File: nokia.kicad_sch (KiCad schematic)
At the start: 21 parts, among them J1 Conn_01x07, J3 Conn_01x04_Pin, J4 Conn_01x04, M1 Motor_DC, SW1 SW_Push, U1 Pico

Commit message: 2nd iteration of board
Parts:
- removed J3: Conn_01x04_Pin, Battery:battery, symbol Connector:Conn_01x04_Pin
- removed J4: Conn_01x04, Connector_PinHeader_2.54mm:PinHeader_1x04_P2.54mm_Vertical, symbol Connector_Generic:Conn_01x04
- removed U1: Pico, MCU_RaspberryPi_and_Boards:RPi_Pico_SMD_TH, symbol MCU_RaspberryPi_and_Boards:Pico
- added C1, C19, C5: 10u, Capacitor_SMD:C_0805_2012Metric, symbol Device:C
- added C10, C6, C7, C9: 4.7u, Capacitor_SMD:C_0402_1005Metric, symbol Device:C
- added C11, C12, C13, C14, C15, C16, C17, C18, C2, C20, C21, C8: 100n, Capacitor_SMD:C_0402_1005Metric, symbol Device:C
- added C3, C4: 15p, Capacitor_SMD:C_0402_1005Metric, symbol Device:C
- added J2: USB_B_Micro, Connector_USB:USB_Micro-B_Amphenol_10103594-0001LF_Horizontal, symbol Connector:USB_B_Micro
- added J20: Conn_01x04_Pin, Battery:battery, symbol Connector:Conn_01x04_Pin
- added J3, J6: SM03B-SRSS-TB, Connector_JST:JST_SH_SM03B-SRSS-TB_1x03-1MP_P1.00mm_Horizontal, symbol Connector_Generic_MountingPin:Conn_01x03_MountingPin
- added J4: Conn_01x06_Pin, Connector:sim connector connector, symbol Connector:SIM_Card
- added J5: Conn_02x06_Top_Bottom, Connector_PinHeader_2.54mm:PinHeader_2x06_P2.54mm_Vertical_SMD, symbol Connector_Generic:Conn_02x06_Top_Bottom
- added JP17: SolderJumper_2_Open, Jumper:SolderJumper-2_P1.3mm_Open_RoundedPad1.0x1.5mm, symbol Jumper:SolderJumper_2_Open
- added KPDOWN1, KPSELECT1, KPUP1: Jumper_2_Open, Jumper:ButtonPads, symbol Jumper:Jumper_2_Open
- added L1: 3.3u, RP2350_80QFN_minimal:L_pol_2016, symbol Device:L
- added R1, R9: DNF, Resistor_SMD:R_0402_1005Metric, symbol Device:R
- added R10: 0, Resistor_SMD:R_0402_1005Metric, symbol Device:R
- added R2, R6: 1k, Resistor_SMD:R_0402_1005Metric, symbol Device:R
- added R3: 33, Resistor_SMD:R_0402_1005Metric, symbol Device:R
- added R7, R8: 27, Resistor_SMD:R_0402_1005Metric, symbol Device:R
- added U1: W25Q128JVS, Package_SO:SOIC-8_5.23x5.23mm_P1.27mm, symbol Memory_Flash:W25Q128JVS
- added U4: NCP1117-3.3_SOT223, Package_TO_SOT_SMD:SOT-223-3_TabPin2, symbol Regulator_Linear:NCP1117-3.3_SOT223
- added U5: RP2350_80QFN, RP2350_80QFN_minimal:RP2350-QFN-80-1EP_10x10_P0.4mm_EP3.4x3.4mm_ThermalVias, symbol MCU_RaspberryPi_RP2350:RP2350_80QFN
- added Y1: ABM8-272-T3, Crystal:Crystal_SMD_3225-4Pin_3.2x2.5mm, symbol Device:Crystal_GND24
- C79: renamed from C1; value C -> 100nF; footprint (none) -> Capacitor_SMD:C_0402_1005Metric
- renumbered JP12 to KP#1, JP10 to KP*1, JP11 to KP0, JP1 to KP1, JP2 to KP2, JP3 to KP3, JP4 to KP4, JP5 to KP5, JP6 to KP6, JP7 to KP7, JP8 to KP8, JP9 to KP9, JP13 to KPC1
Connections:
- net +3V3: now also KP#1.1 (A), KP*1.1 (A), KP1.1 (A), KP2.1 (A), KP3.1 (A), KP4.1 (A), KP6.1 (A), KP7.1 (A), KP8.1 (A), KP9.1 (A), C12.1, C13.1, C14.1, C15.1, C16.1, C17.1, C18.1, C19.1, C2.1, C20.1, C21.1, C5.1, C6.1, J20.1 (Pin_1), J4.1 (VCC), KPDOWN1.1 (A), KPSELECT1.1 (A), KPUP1.1 (A), R1.1, R3.1, U1.8 (VCC), U4.2 (VO), U5.15 (IOVDD), U5.24 (IOVDD), U5.29 (IOVDD), U5.41 (IOVDD), U5.5 (IOVDD), U5.50 (IOVDD), U5.59 (ADC_AVDD), U5.60 (IOVDD), U5.64 (VREG_VIN), U5.68 (USB_OTP_VDD), U5.69 (QSPI_IOVDD), U5.76 (IOVDD); no longer KP#1.2 (B), KP*1.2 (B), KP1.2 (B), KP2.2 (B), KP3.2 (B), KP4.2 (B), KP6.2 (B), KP7.2 (B), KP8.2 (B), KP9.2 (B)
- net GND: now also LS2.2, M1.2 (-), C1.2, C10.2, C11.2, C12.2, C13.2, C14.2, C15.2, C16.2, C17.2, C18.2, C19.2, C2.2, C20.2, C21.2, C3.2, C4.2, C5.2, C6.2, C7.2, C8.2, C9.2, J2.5 (GND), J2.6 (Shield), J20.4 (Pin_4), J3.2 (Pin_2), J3.MP (MountPin), J4.5 (GND), J5.9 (Pin_9), J6.2 (Pin_2), J6.MP (MountPin), R6.2, U1.4 (GND), U4.1 (GND), U5.62 (VREG_PGND), U5.81 (GND), Y1.2, Y1.4; no longer SW1.1
- net GPIO16: now reaches KPC1.2 (B)
- net GPIO16: now also U5.16 (GPIO16)
- net GPIO33: now reaches J1.8 (Pin_8)
- net GPIO33: now also J5.7 (Pin_7), U5.42 (GPIO33)
- net GPIO10: now reaches KP0.2 (B)
- net GPIO10: now also U5.8 (GPIO10)
- net GPIO36: now reaches J1.4 (Pin_4)
- net GPIO36: now also J5.11 (Pin_11), U5.45 (GPIO36)
- net GPIO37: now reaches J1.5 (Pin_5)
- net GPIO37: now also J5.10 (Pin_10), U5.46 (GPIO37)
- net GPIO38: now reaches J1.2 (Pin_2)
- net GPIO38: now also U5.47 (GPIO38)
- net GPIO39: now reaches J1.3 (Pin_3)
- net GPIO39: now also J5.12 (Pin_12), U5.48 (GPIO39)
- net RUN: now reaches SW1.2
- net RUN: now also U5.35 (RUN)
- net GPIO2: now reaches M1.1 (+)
- net GPIO2: now also U5.79 (GPIO2)
- net GPIO21: now reaches LS2.1
- net GPIO21: now also U5.21 (GPIO21)
- net GPIO14: now reaches KP5.2 (B)
- net GPIO14: now also U5.13 (GPIO14)
- net at J1.7 (Pin_7): now also J5.8 (Pin_8), JP17.1 (A); no longer C79.2
- new net: R8.2, U5.66 (USB_DM)
- new net: C4.1, R2.2, Y1.3
- new net: R6.1, SW1.1
- new net: C79.2, JP17.2 (B)
- new net: R7.2, U5.67 (USB_DP)
- new net +1V1: C10.1, C11.1, C7.1, C8.1, L1.1, U5.10 (DVDD), U5.32 (DVDD), U5.51 (DVDD), U5.65 (VREG_FB)
- new net FLASH_SS: R1.2, R10.2, R9.2, U1.1 (~{CS})
- new net GPIO0: J3.3 (Pin_3), R9.1, U5.77 (GPIO0)
- new net GPIO1: J3.1 (Pin_1), U5.78 (GPIO1)
- new net GPIO11: KP8.2 (B), U5.9 (GPIO11)
- new net GPIO12: KPSELECT1.2 (B), U5.11 (GPIO12)
- new net GPIO13: KP2.2 (B), U5.12 (GPIO13)
- new net GPIO15: J4.3 (CLK), U5.14 (GPIO15)
- new net GPIO17: KP1.2 (B), U5.17 (GPIO17)
- new net GPIO18: KP4.2 (B), U5.18 (GPIO18)
- new net GPIO19: KP7.2 (B), U5.19 (GPIO19)
- new net GPIO20: KP*1.2 (B), U5.20 (GPIO20)
- new net GPIO22: J4.7 (I/O), U5.22 (GPIO22)
- new net GPIO23: J4.2 (RST), U5.23 (GPIO23)
- new net GPIO24: U5.25 (GPIO24)
- new net GPIO25: U5.26 (GPIO25)
- new net GPIO26: U5.27 (GPIO26)
- new net GPIO27: U5.28 (GPIO27)
- new net GPIO28: U5.36 (GPIO28)
- new net GPIO29: U5.37 (GPIO29)
- new net GPIO3: U5.80 (GPIO3)
- new net GPIO30: U5.38 (GPIO30)
- new net GPIO31: U5.39 (GPIO31)
- new net GPIO32: U5.40 (GPIO32)
- new net GPIO34: U5.43 (GPIO34)
- new net GPIO35: U5.44 (GPIO35)
- new net GPIO4: KP#1.2 (B), U5.1 (GPIO4)
- new net GPIO40_ADC0: U5.49 (GPIO40_ADC0)
- new net GPIO41_ADC1: U5.52 (GPIO41_ADC1)
- new net GPIO42_ADC2: U5.53 (GPIO42_ADC2)
- new net GPIO43_ADC3: U5.54 (GPIO43_ADC3)
- new net GPIO44_ADC4: U5.55 (GPIO44_ADC4)
- new net GPIO45_ADC5: U5.56 (GPIO45_ADC5)
- new net GPIO46_ADC6: U5.57 (GPIO46_ADC6)
- new net GPIO47_ADC7: U5.58 (GPIO47_ADC7)
- new net GPIO5: KP9.2 (B), U5.2 (GPIO5)
- new net GPIO6: KP6.2 (B), U5.3 (GPIO6)
- new net GPIO7: KP3.2 (B), U5.4 (GPIO7)
- new net GPIO8: KPDOWN1.2 (B), U5.6 (GPIO8)
- new net GPIO9: KPUP1.2 (B), U5.7 (GPIO9)
- new net QSPI_SCLK: U1.6 (CLK), U5.71 (QSPI_SCLK)
- new net QSPI_SD0: U1.5 (DI(IO0)), U5.72 (QSPI_SD0)
- new net QSPI_SD1: U1.2 (DO(IO1)), U5.74 (QSPI_SD1)
- new net QSPI_SD2: U1.3 (IO2), U5.73 (QSPI_SD2)
- new net QSPI_SD3: U1.7 (IO3), U5.70 (QSPI_SD3)
- new net QSPI_SS: R10.1, U5.75 (QSPI_SS)
- new net SWCLK: J6.1 (Pin_1), U5.33 (SWCLK)
- new net SWD: J6.3 (Pin_3), U5.34 (SWD)
- new net USB_D+: J2.3 (D+), R7.1
- new net USB_D-: J2.2 (D-), R8.1
- new net VBUS: C1.1, J2.1 (VBUS), U4.3 (VI)
- new net VREG_AVDD: C9.1, R3.2, U5.61 (VREG_AVDD)
- new net VREG_LX: L1.2, U5.63 (VREG_LX)
- new net XIN: C3.1, U5.30 (XIN), Y1.1
- new net XOUT: R2.1, U5.31 (XOUT)
- no-connect marks 0 -> 3
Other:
- note added: "12MHz Crystal"
- note added: "Battery Connection"
- note added: "Display and Misc. GPIO Connection"
- note added: "Flash"
- note added: "JST Debug Connector"
- note added: "Keypad"
- note added: "Make sure R7 and R8 are close to RP2350"
- note added: "Power"
- note added: "SIM Card Tray Connector"
- note added: "UART Connector"
- moved on the sheet: C79, J1, KP#1, KP*1, KP0, KP1, KP2, KP3, KP4, KP5, KP6, KP7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

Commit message: 2nd iteration of board
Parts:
- removed J5: Conn_02x06_Top_Bottom, Connector_PinHeader_2.54mm:PinHeader_2x06_P2.54mm_Vertical_SMD, symbol Connector_Generic:Conn_02x06_Top_Bottom
- added D1: D, symbol Device:D
- added D2, D3, D4, D5, D6, D7, D8, D9: LED_ARGB, LED_SMD:RGBLED-reverse, symbol Device:LED_ARGB
- added Q1: BC847, Package_TO_SOT_SMD:SOT-23, symbol Transistor_BJT:BC847
- added R11, R12, R14, R15, R16, R17, R19, R20, R22, R23, R25, R26, R28, R29, R31, R32: 90, Resistor_SMD:R_0402_1005Metric, symbol Device:R
- added R13, R18, R21, R24, R27, R30, R4, R5: 140, Resistor_SMD:R_0402_1005Metric, symbol Device:R
- LS2: value Speaker_Crystal -> Buzzer
- M1: value Motor_DC -> Vibration
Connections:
- net +3V3: now also M1.1 (+), D1.1 (K), D2.2, D3.2 (A), D4.2 (A), D5.2 (A), D6.2 (A), D7.2 (A), D8.2 (A), D9.2 (A)
- net GND: now also Q1.2 (E); no longer M1.2 (-)
- net GPIO2: now also Q1.1 (B); no longer M1.1 (+)
- net GPIO30: now also R13.2, R18.2, R21.2, R24.2, R27.2, R30.2, R4.2, R5.2
- net GPIO32: now also R11.1, R14.1, R16.1, R19.1, R22.1, R25.1, R28.1, R31.1
- net GPIO34: now also R12.1, R15.1, R17.1, R20.1, R23.1, R26.1, R29.1, R32.1
- new net: D5.3 (GK), R31.2
- new net: D4.4 (BK), R29.2
- new net: D5.4 (BK), R32.2
- new net: D6.3 (GK), R16.2
- new net: D7.4 (BK), R12.2
- new net: D1.2 (A), M1.2 (-), Q1.3 (C)
- new net: D3.1 (RK), R24.1
- new net: D8.1 (RK), R18.1
- new net: D8.3 (GK), R19.2
- new net: D8.4 (BK), R20.2
- new net: D4.1 (RK), R27.1
- new net: D9.4 (BK), R15.2
- new net: D2.1, R21.1
- new net: D2.3 (GK), R22.2
- new net: D2.4 (BK), R23.2
- new net: D3.3 (GK), R25.2
- new net: D3.4 (BK), R26.2
- new net: D4.3 (GK), R28.2
- new net: D5.1 (RK), R30.1
- new net: D7.1 (RK), R4.1
- new net: D7.3 (GK), R11.2
- new net: D6.1 (RK), R5.1
- new net: D6.4 (BK), R17.2
- new net: D9.1 (RK), R13.1
- new net: D9.3 (GK), R14.2
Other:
- moved on the sheet: C1, C2, C3, C4, C5, C79, J2, J20, J3, J4, J6, JP17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

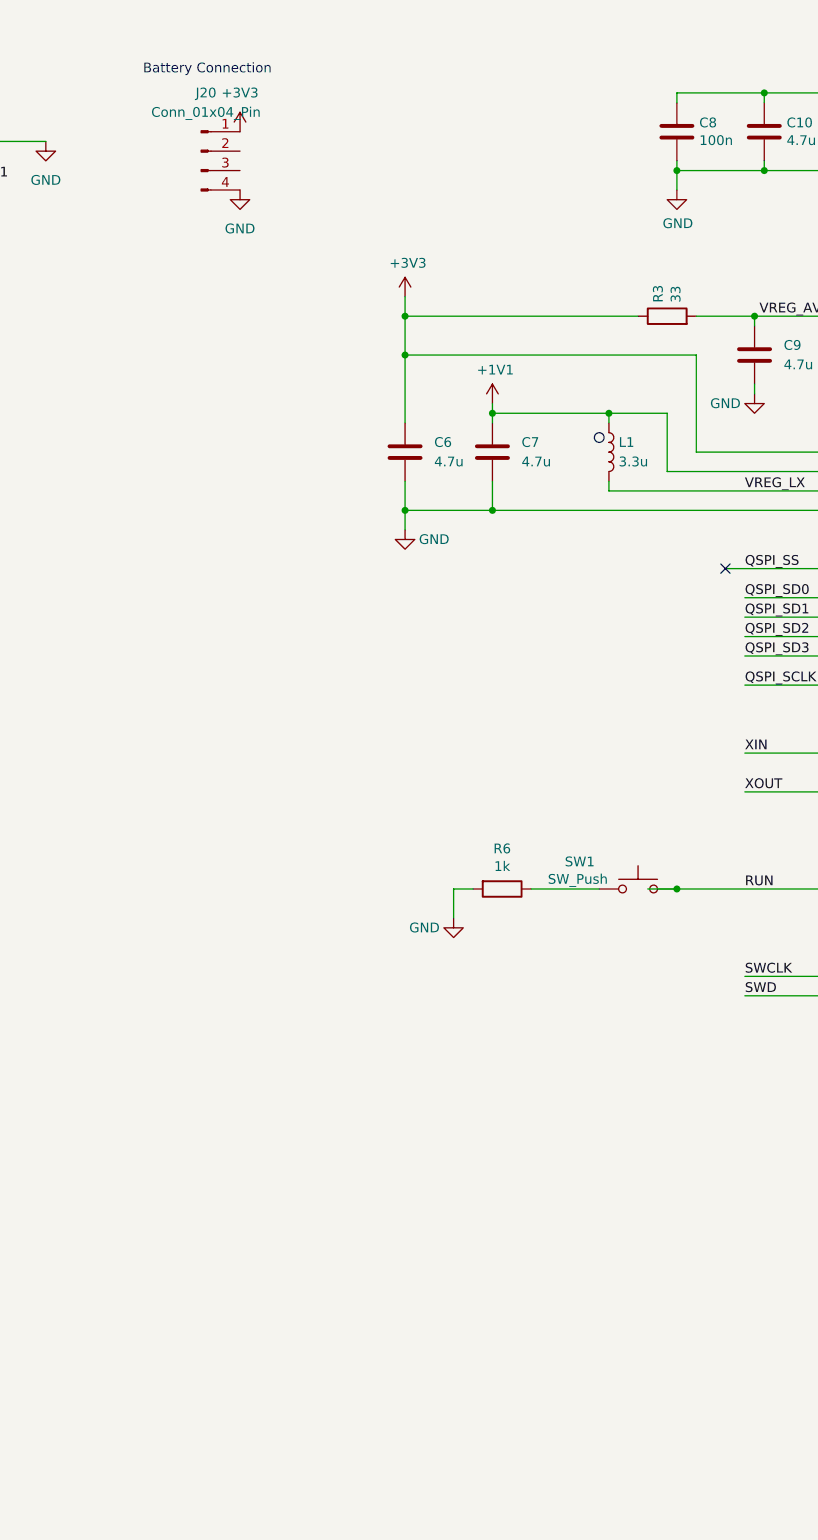
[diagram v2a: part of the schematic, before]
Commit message: add breakout connector
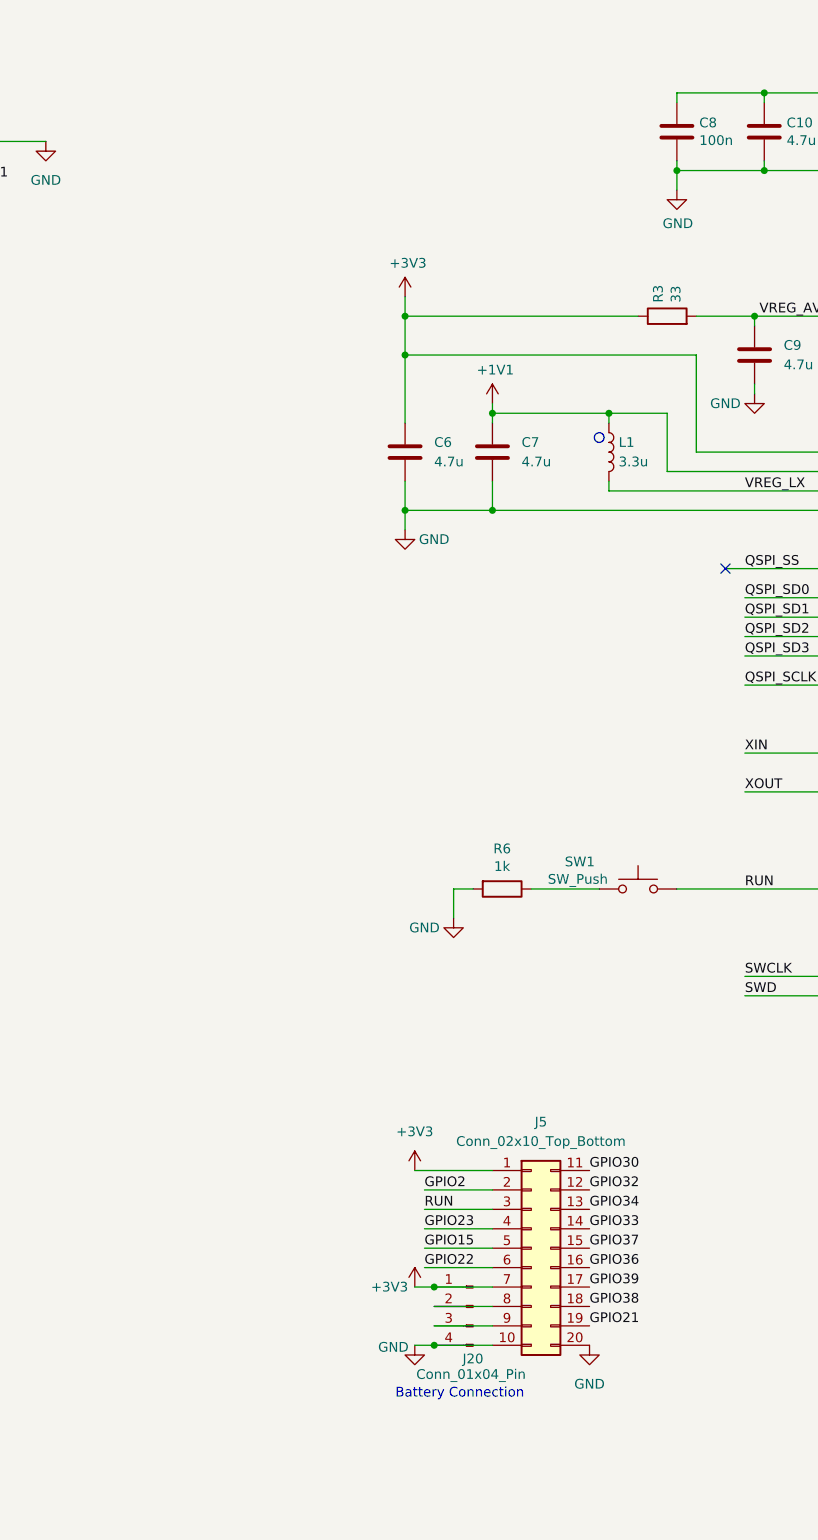
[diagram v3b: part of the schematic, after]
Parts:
- added J5: Conn_02x10_Top_Bottom, Connector_PinHeader_2.54mm:PinHeader_2x10_P2.54mm_Vertical_SMD, symbol Connector_Generic:Conn_02x10_Top_Bottom
- D1: footprint (none) -> Diode_SMD:D_0402_1005Metric
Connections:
- net +3V3: now also J5.1 (Pin_1), J5.7 (Pin_7)
- net GND: now also J5.10 (Pin_10), J5.20 (Pin_20)
- net GPIO15: now also J5.5 (Pin_5)
- net GPIO2: now also J5.2 (Pin_2)
- net GPIO21: now also J5.19 (Pin_19)
- net GPIO22: now also J5.6 (Pin_6)
- net GPIO23: now also J5.4 (Pin_4)
- net GPIO30: now also J5.11 (Pin_11)
- net GPIO32: now also J5.12 (Pin_12)
- net GPIO33: now also J5.14 (Pin_14)
- net GPIO34: now also J5.13 (Pin_13)
- net GPIO36: now also J5.16 (Pin_16)
- net GPIO37: now also J5.15 (Pin_15)
- net GPIO38: now also J5.18 (Pin_18)
- net GPIO39: now also J5.17 (Pin_17)
- net RUN: now also J5.3 (Pin_3)
- net at J20.2 (Pin_2): now also J5.8 (Pin_8)
- net at J20.3 (Pin_3): now also J5.9 (Pin_9)
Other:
- moved on the sheet: J20
